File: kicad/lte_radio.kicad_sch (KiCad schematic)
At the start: 24 parts, among them J11 JAE_SIM_Card_SF72S006, J13 Conn_01x06, J14 Conn_01x06, Q1 2N7002, U24 MONARCH_2_GM02S, U26 TXB0108DQSR

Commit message: assign footprints
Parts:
- C92, C93, C94, C95, C96: footprint (none) -> Capacitor_SMD:C_0603_1608Metric_Pad1.08x0.95mm_HandSolder
- R115, R116, R117, R118, R119, R120, R121, R122, R123, R124, R125: footprint (none) -> Resistor_SMD:R_0603_1608Metric_Pad0.98x0.95mm_HandSolder
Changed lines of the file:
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@@
       (effects (font (size 1.27 1.27)) (justify left))
     )
-    (property "Footprint" "" (at 257.556 131.064 90)
+    (property "Footprint" "Resistor_SMD:R_0603_1608Metric_Pad0.98x0.95mm_HandSolder" (at 257.556 131.064 90)
       (effects (font (size 1.27 1.27)) hide)
     )
@@
       (effects (font (size 1.27 1.27)) (justify left))
     )
-    (property "Footprint" "" (at 271.526 131.064 90)
+    (property "Footprint" "Resistor_SMD:R_0603_1608Metric_Pad0.98x0.95mm_HandSolder" (at 271.526 131.064 90)
       (effects (font (size 1.27 1.27)) hide)
     )
@@
       (effects (font (size 1.27 1.27)) (justify left))
     )
-    (property "Footprint" "" (at 106.426 103.124 90)
+    (property "Footprint" "Resistor_SMD:R_0603_1608Metric_Pad0.98x0.95mm_HandSolder" (at 106.426 103.124 90)
       (effects (font (size 1.27 1.27)) hide)
     )
@@
       (effects (font (size 1.27 1.27)) (justify left))
     )
-    (property "Footprint" "" (at 73.3552 110.49 0)
+    (property "Footprint" "Capacitor_SMD:C_0603_1608Metric_Pad1.08x0.95mm_HandSolder" (at 73.3552 110.49 0)
       (effects (font (size 1.27 1.27)) hide)
     )
@@
       (effects (font (size 1.27 1.27)) (justify left))
     )
-    (property "Footprint" "" (at 299.4152 128.27 0)
+    (property "Footprint" "Capacitor_SMD:C_0603_1608Metric_Pad1.08x0.95mm_HandSolder" (at 299.4152 128.27 0)
       (effects (font (size 1.27 1.27)) hide)
     )
@@
       (effects (font (size 1.27 1.27)) (justify left))
     )
-    (property "Footprint" "" (at 128.016 174.244 90)
+    (property "Footprint" "Resistor_SMD:R_0603_1608Metric_Pad0.98x0.95mm_HandSolder" (at 128.016 174.244 90)
       (effects (font (size 1.27 1.27)) hide)
     )
@@
       (effects (font (size 1.27 1.27)) (justify left))
     )
-    (property "Footprint" "" (at 87.376 103.124 90)
+    (property "Footprint" "Resistor_SMD:R_0603_1608Metric_Pad0.98x0.95mm_HandSolder" (at 87.376 103.124 90)
       (effects (font (size 1.27 1.27)) hide)
     )
@@
       (effects (font (size 1.27 1.27)) (justify left))
     )
-    (property "Footprint" "" (at 46.6852 107.95 0)
+    (property "Footprint" "Capacitor_SMD:C_0603_1608Metric_Pad1.08x0.95mm_HandSolder" (at 46.6852 107.95 0)
       (effects (font (size 1.27 1.27)) hide)
     )
@@
       (effects (font (size 1.27 1.27)) (justify left))
     )
-    (property "Footprint" "" (at 96.266 103.124 90)
+    (property "Footprint" "Resistor_SMD:R_0603_1608Metric_Pad0.98x0.95mm_HandSolder" (at 96.266 103.124 90)
       (effects (font (size 1.27 1.27)) hide)
     )
@@
       (effects (font (size 1.27 1.27)) (justify left))
     )
-    (property "Footprint" "" (at 404.8252 88.9 0)
+    (property "Footprint" "Capacitor_SMD:C_0603_1608Metric_Pad1.08x0.95mm_HandSolder" (at 404.8252 88.9 0)
       (effects (font (size 1.27 1.27)) hide)
     )
@@
       (effects (font (size 1.27 1.27)))
     )
-    (property "Footprint" "" (at 298.704 81.534 90)
+    (property "Footprint" "Resistor_SMD:R_0603_1608Metric_Pad0.98x0.95mm_HandSolder" (at 298.704 81.534 90)
       (effects (font (size 1.27 1.27)) hide)
     )
@@
       (effects (font (size 1.27 1.27)))
     )
-    (property "Footprint" "" (at 282.194 129.794 90)
+    (property "Footprint" "Resistor_SMD:R_0603_1608Metric_Pad0.98x0.95mm_HandSolder" (at 282.194 129.794 90)
       (effects (font (size 1.27 1.27)) hide)
     )
@@
       (effects (font (size 1.27 1.27)) (justify left))
     )
-    (property "Footprint" "" (at 291.846 87.884 90)
+    (property "Footprint" "Resistor_SMD:R_0603_1608Metric_Pad0.98x0.95mm_HandSolder" (at 291.846 87.884 90)
       (effects (font (size 1.27 1.27)) hide)
     )
@@
       (effects (font (size 1.27 1.27)) (justify left))
     )
-    (property "Footprint" "" (at 307.086 87.884 90)
+    (property "Footprint" "Resistor_SMD:R_0603_1608Metric_Pad0.98x0.95mm_HandSolder" (at 307.086 87.884 90)
       (effects (font (size 1.27 1.27)) hide)
     )
@@
       (effects (font (size 1.27 1.27)) (justify left))
     )
-    (property "Footprint" "" (at 133.096 103.124 90)
+    (property "Footprint" "Resistor_SMD:R_0603_1608Metric_Pad0.98x0.95mm_HandSolder" (at 133.096 103.124 90)
       (effects (font (size 1.27 1.27)) hide)
     )
@@
       (effects (font (size 1.27 1.27)) (justify left))
     )
-    (property "Footprint" "" (at 87.3252 118.11 0)
-      (effects (font (size 1.27 1.27)) hide)
-    )
+    (property "Footprint" "Capacitor_SMD:C_0603_1608Metric_Pad1.08x0.95mm_HandSolder" (at 87.3252 118.11 0)
+      (effects (font (size 1.27 1.27)) hide)
+    )

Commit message: fix ercs
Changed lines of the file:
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@@
   (junction (at 387.35 147.32) (diameter 0) (color 0 0 0 0)
+  )
+  (junction (at 242.57 138.43) (diameter 0) (color 0 0 0 0)
   )
   (junction (at 356.87 160.02) (diameter 0) (color 0 0 0 0)
@@
     (stroke (width 0) (type default))
   )
+  (wire (pts (xy 242.57 138.43) (xy 276.86 138.43))
+    (stroke (width 0) (type default))
+  )
   (wire (pts (xy 125.73 113.03) (xy 149.86 113.03))
     (stroke (width 0) (type default))
@@
     (stroke (width 0) (type default))
   )
-  (wire (pts (xy 236.22 138.43) (xy 276.86 138.43))
+  (wire (pts (xy 236.22 138.43) (xy 242.57 138.43))
     (stroke (width 0) (type default))
   )
@@
         )
       )
+    )
+  )
+  (symbol (lib_id "power:PWR_FLAG") (at 242.57 138.43 0) (unit 1)
+    (in_bom yes) (on_board yes) (dnp no) (fields_autoplaced)
+    (property "Reference" "#FLG05" (at 242.57 136.525 0)
+      (effects (font (size 1.27 1.27)) hide)
+    )
+    (property "Value" "PWR_FLAG" (at 242.57 133.35 0)
+      (effects (font (size 1.27 1.27)))
+    )
+    (property "Footprint" "" (at 242.57 138.43 0)
+      (effects (font (size 1.27 1.27)) hide)
+    )
+    (property "Datasheet" "~" (at 242.57 138.43 0)
+      (effects (font (size 1.27 1.27)) hide)
+    )
+    (pin "1")
+    (instances
+      (project "gpsrx"
+        (path "/c3c549bc-9d82-4b6a-bdb9-a3870905229d/c578a973-c3ec-43d9-a435-a55d342147d7"
+          (reference "#FLG05") (unit 1)
+        )
+      )

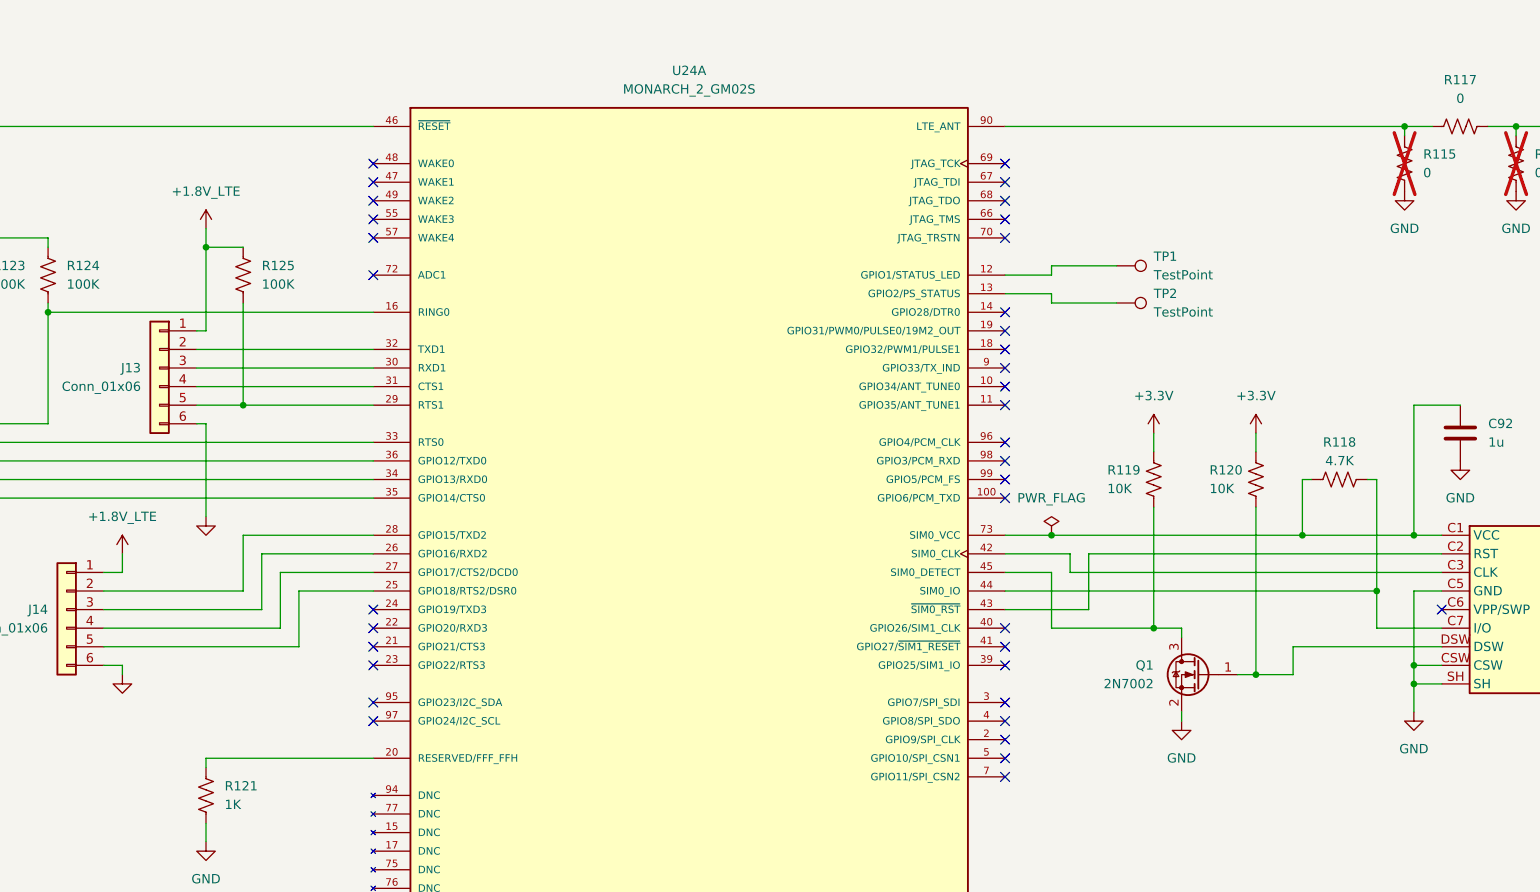
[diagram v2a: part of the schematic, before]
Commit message: add net names
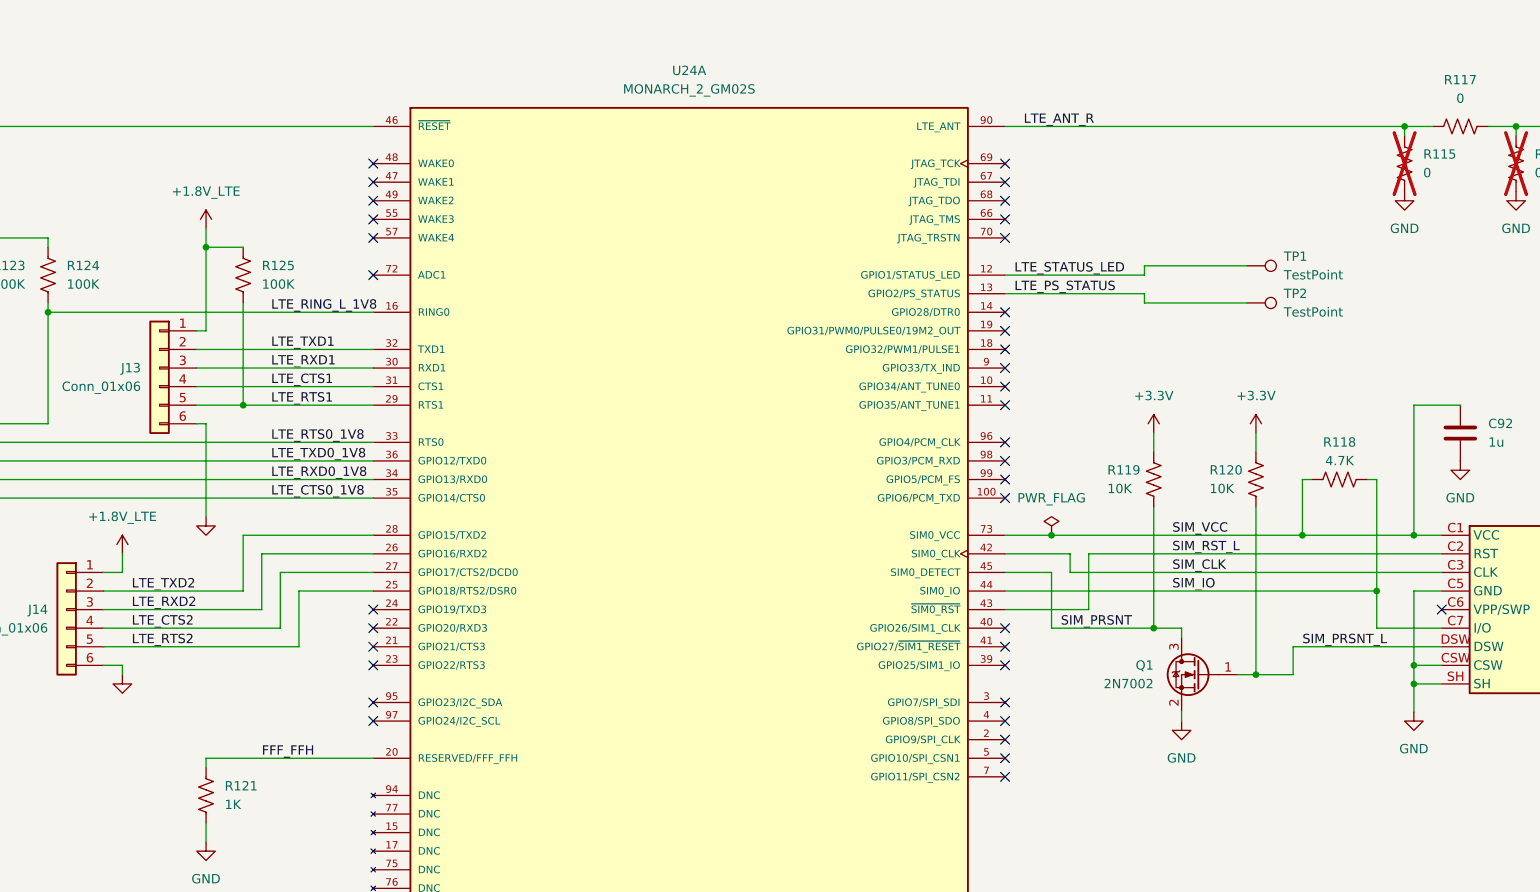
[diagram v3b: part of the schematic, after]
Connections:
- net SIM_PRSNT: now reaches Q1.3 (D), R119.2, U24.45 (SIM0_DETECT)
- net SIM_PRSNT_L: now reaches J11.DSW, Q1.1 (G), R120.2
- net LTE_RING_L_1V8: now reaches R124.2, U24.16 (RING0), U26.1 (A1)
- net LTE_RTS0_1V8: now reaches R123.2, U24.33 (RTS0), U26.2 (A2)
- net LTE_TXD0_1V8: now reaches U24.36 (GPIO12/TXD0), U26.3 (A3)
- net LTE_RXD0_1V8: now reaches U24.34 (GPIO13/RXD0), U26.4 (A4)
- net LTE_CTS0_1V8: now reaches U24.35 (GPIO14/CTS0), U26.7 (A5)
- net SIM_VCC: now reaches C92.1, J11.C1 (VCC), R118.1, U24.73 (SIM0_VCC)
- net FFF_FFH: now reaches R121.1, U24.20 (RESERVED/FFF_FFH)
- net LTE_TXD2: now reaches J14.2 (Pin_2), U24.28 (GPIO15/TXD2)
- net LTE_RXD2: now reaches J14.3 (Pin_3), U24.26 (GPIO16/RXD2)
- net LTE_CTS2: now reaches J14.4 (Pin_4), U24.27 (GPIO17/CTS2/DCD0)
- net LTE_RTS2: now reaches J14.5 (Pin_5), U24.25 (GPIO18/RTS2/DSR0)
- net LTE_STATUS_LED: now reaches TP1.1, U24.12 (GPIO1/STATUS_LED)
- net LTE_PS_STATUS: now reaches TP2.1, U24.13 (GPIO2/PS_STATUS)
- net LTE_RTS1: now reaches J13.5 (Pin_5), R125.2, U24.29 (RTS1)
- net LTE_RXD1: now reaches J13.3 (Pin_3), U24.30 (RXD1)
- net LTE_CTS1: now reaches J13.4 (Pin_4), U24.31 (CTS1)
- net LTE_TXD1: now reaches J13.2 (Pin_2), U24.32 (TXD1)
- net SIM_CLK: now reaches J11.C3 (CLK), U24.42 (SIM0_CLK)
- net SIM_RST_L: now reaches J11.C2 (RST), U24.43 (~{SIM0_RST})
- net SIM_IO: now reaches J11.C7 (I/O), R118.2, U24.44 (SIM0_IO)
- net LTE_ANT_R: now reaches R115.1, R117.1, U24.90 (LTE_ANT)
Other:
- moved on the sheet: TP1, TP2
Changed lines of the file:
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@@
     (stroke (width 0) (type default))
   )
-  (wire (pts (xy 242.57 106.68) (xy 251.46 106.68))
+  (wire (pts (xy 255.27 106.68) (xy 269.24 106.68))
     (stroke (width 0) (type default))
   )
@@
     (stroke (width 0) (type default))
   )
-  (wire (pts (xy 236.22 105.41) (xy 242.57 105.41))
+  (wire (pts (xy 236.22 105.41) (xy 255.27 105.41))
     (stroke (width 0) (type default))
   )
@@
     (stroke (width 0) (type default))
   )
-  (wire (pts (xy 236.22 102.87) (xy 242.57 102.87))
+  (wire (pts (xy 236.22 102.87) (xy 255.27 102.87))
     (stroke (width 0) (type default))
   )
@@
     (stroke (width 0) (type default))
   )
-  (wire (pts (xy 242.57 101.6) (xy 251.46 101.6))
+  (wire (pts (xy 255.27 101.6) (xy 269.24 101.6))
     (stroke (width 0) (type default))
   )
@@
     (stroke (width 0) (type default))
   )
-  (wire (pts (xy 242.57 102.87) (xy 242.57 101.6))
+  (wire (pts (xy 255.27 102.87) (xy 255.27 101.6))
     (stroke (width 0) (type default))
   )
@@
     (stroke (width 0) (type default))
   )
-  (wire (pts (xy 242.57 105.41) (xy 242.57 106.68))
+  (wire (pts (xy 255.27 105.41) (xy 255.27 106.68))
     (stroke (width 0) (type default))
   )
@@
   (wire (pts (xy 356.87 127) (xy 356.87 129.54))
     (stroke (width 0) (type default))
+  )
+  (label "SIM_RST_L" (at 259.08 140.97 0) (fields_autoplaced)
+    (effects (font (size 1.27 1.27)) (justify left bottom))
+  )
+  (label "SIM_PRSNT" (at 243.84 151.13 0) (fields_autoplaced)
+    (effects (font (size 1.27 1.27)) (justify left bottom))
+  )
+  (label "LTE_ANT_R" (at 238.76 82.55 0) (fields_autoplaced)
+    (effects (font (size 1.27 1.27)) (justify left bottom))
+  )
+  (label "LTE_CTS2" (at 116.84 151.13 0) (fields_autoplaced)
+    (effects (font (size 1.27 1.27)) (justify left bottom))
+  )
+  (label "LTE_RING_L_1V8" (at 135.89 107.95 0) (fields_autoplaced)
+    (effects (font (size 1.27 1.27)) (justify left bottom))
+  )
+  (label "LTE_CTS1" (at 135.89 118.11 0) (fields_autoplaced)
+    (effects (font (size 1.27 1.27)) (justify left bottom))
+  )
+  (label "LTE_STATUS_LED" (at 237.49 102.87 0) (fields_autoplaced)
+    (effects (font (size 1.27 1.27)) (justify left bottom))
+  )
+  (label "LTE_RTS0_1V8" (at 135.89 125.73 0) (fields_autoplaced)
+    (effects (font (size 1.27 1.27)) (justify left bottom))
+  )
+  (label "LTE_RTS1" (at 135.89 120.65 0) (fields_autoplaced)
+    (effects (font (size 1.27 1.27)) (justify left bottom))
+  )
+  (label "SIM_IO" (at 259.08 146.05 0) (fields_autoplaced)
+    (effects (font (size 1.27 1.27)) (justify left bottom))
+  )
+  (label "LTE_RXD2" (at 116.84 148.59 0) (fields_autoplaced)
+    (effects (font (size 1.27 1.27)) (justify left bottom))
+  )
+  (label "LTE_CTS0_1V8" (at 135.89 133.35 0) (fields_autoplaced)
+    (effects (font (size 1.27 1.27)) (justify left bottom))
+  )
+  (label "FFF_FFH" (at 134.62 168.91 0) (fields_autoplaced)
+    (effects (font (size 1.27 1.27)) (justify left bottom))
+  )
+  (label "SIM_CLK" (at 259.08 143.51 0) (fields_autoplaced)
+    (effects (font (size 1.27 1.27)) (justify left bottom))
+  )
+  (label "LTE_TXD2" (at 116.84 146.05 0) (fields_autoplaced)
+    (effects (font (size 1.27 1.27)) (justify left bottom))
+  )
+  (label "LTE_TXD0_1V8" (at 135.89 128.27 0) (fields_autoplaced)
+    (effects (font (size 1.27 1.27)) (justify left bottom))
+  )
+  (label "LTE_RTS2" (at 116.84 153.67 0) (fields_autoplaced)
+    (effects (font (size 1.27 1.27)) (justify left bottom))
+  )
+  (label "LTE_TXD1" (at 135.89 113.03 0) (fields_autoplaced)
+    (effects (font (size 1.27 1.27)) (justify left bottom))
+  )
+  (label "LTE_PS_STATUS" (at 237.49 105.41 0) (fields_autoplaced)
+    (effects (font (size 1.27 1.27)) (justify left bottom))
+  )
+  (label "LTE_RXD1" (at 135.89 115.57 0) (fields_autoplaced)
+    (effects (font (size 1.27 1.27)) (justify left bottom))
+  )
+  (label "SIM_VCC" (at 259.08 138.43 0) (fields_autoplaced)
+    (effects (font (size 1.27 1.27)) (justify left bottom))
+  )
+  (label "LTE_RXD0_1V8" (at 135.89 130.81 0) (fields_autoplaced)
+    (effects (font (size 1.27 1.27)) (justify left bottom))
+  )
+  (label "SIM_PRSNT_L" (at 276.86 153.67 0) (fields_autoplaced)
+    (effects (font (size 1.27 1.27)) (justify left bottom))
   )
   (global_label "LTE_ANT" (shape bidirectional) (at 317.5 82.55 0) (fields_autoplaced)
@@
     )
   )
-  (symbol (lib_id "Connector:TestPoint") (at 251.46 106.68 270) (unit 1)
-    (in_bom yes) (on_board yes) (dnp no) (fields_autoplaced)
-    (property "Reference" "TP2" (at 256.54 105.41 90)
-      (effects (font (size 1.27 1.27)) (justify left))
-    )
-    (property "Value" "TestPoint" (at 256.54 107.95 90)
-      (effects (font (size 1.27 1.27)) (justify left))
-    )
-    (property "Footprint" "TestPoint:TestPoint_Pad_D1.0mm" (at 251.46 111.76 0)
-      (effects (font (size 1.27 1.27)) hide)
-    )
-    (property "Datasheet" "~" (at 251.46 111.76 0)
+  (symbol (lib_id "Connector:TestPoint") (at 269.24 106.68 270) (unit 1)
+    (in_bom yes) (on_board yes) (dnp no) (fields_autoplaced)
+    (property "Reference" "TP2" (at 274.32 105.41 90)
+      (effects (font (size 1.27 1.27)) (justify left))
+    )
+    (property "Value" "TestPoint" (at 274.32 107.95 90)
+      (effects (font (size 1.27 1.27)) (justify left))
+    )
+    (property "Footprint" "TestPoint:TestPoint_Pad_D1.0mm" (at 269.24 111.76 0)
+      (effects (font (size 1.27 1.27)) hide)
+    )
+    (property "Datasheet" "~" (at 269.24 111.76 0)
       (effects (font (size 1.27 1.27)) hide)
     )
@@
     )
   )
-  (symbol (lib_id "Connector:TestPoint") (at 251.46 101.6 270) (unit 1)
-    (in_bom yes) (on_board yes) (dnp no) (fields_autoplaced)
-    (property "Reference" "TP1" (at 256.54 100.33 90)
-      (effects (font (size 1.27 1.27)) (justify left))
-    )
-    (property "Value" "TestPoint" (at 256.54 102.87 90)
-      (effects (font (size 1.27 1.27)) (justify left))
-    )
-    (property "Footprint" "TestPoint:TestPoint_Pad_D1.0mm" (at 251.46 106.68 0)
-      (effects (font (size 1.27 1.27)) hide)
-    )
-    (property "Datasheet" "~" (at 251.46 106.68 0)
-      (effects (font (size 1.27 1.27)) hide)
-    )
+  (symbol (lib_id "Connector:TestPoint") (at 269.24 101.6 270) (unit 1)
+    (in_bom yes) (on_board yes) (dnp no) (fields_autoplaced)
+    (property "Reference" "TP1" (at 274.32 100.33 90)
+      (effects (font (size 1.27 1.27)) (justify left))
+    )
+    (property "Value" "TestPoint" (at 274.32 102.87 90)
+      (effects (font (size 1.27 1.27)) (justify left))
+    )
+    (property "Footprint" "TestPoint:TestPoint_Pad_D1.0mm" (at 269.24 106.68 0)
+      (effects (font (size 1.27 1.27)) hide)
+    )
+    (property "Datasheet" "~" (at 269.24 106.68 0)
+      (effects (font (size 1.27 1.27)) hide)
+    )
